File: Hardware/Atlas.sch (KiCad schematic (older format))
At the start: 47 parts, among them J1 DC, U1 MS5611, U2 HTU21D, U3 uSD Card, U4 RFD900, U5 MPU9150, U6 XBEE, U7 VENUS838FLPX-L, U8 AOZ1031

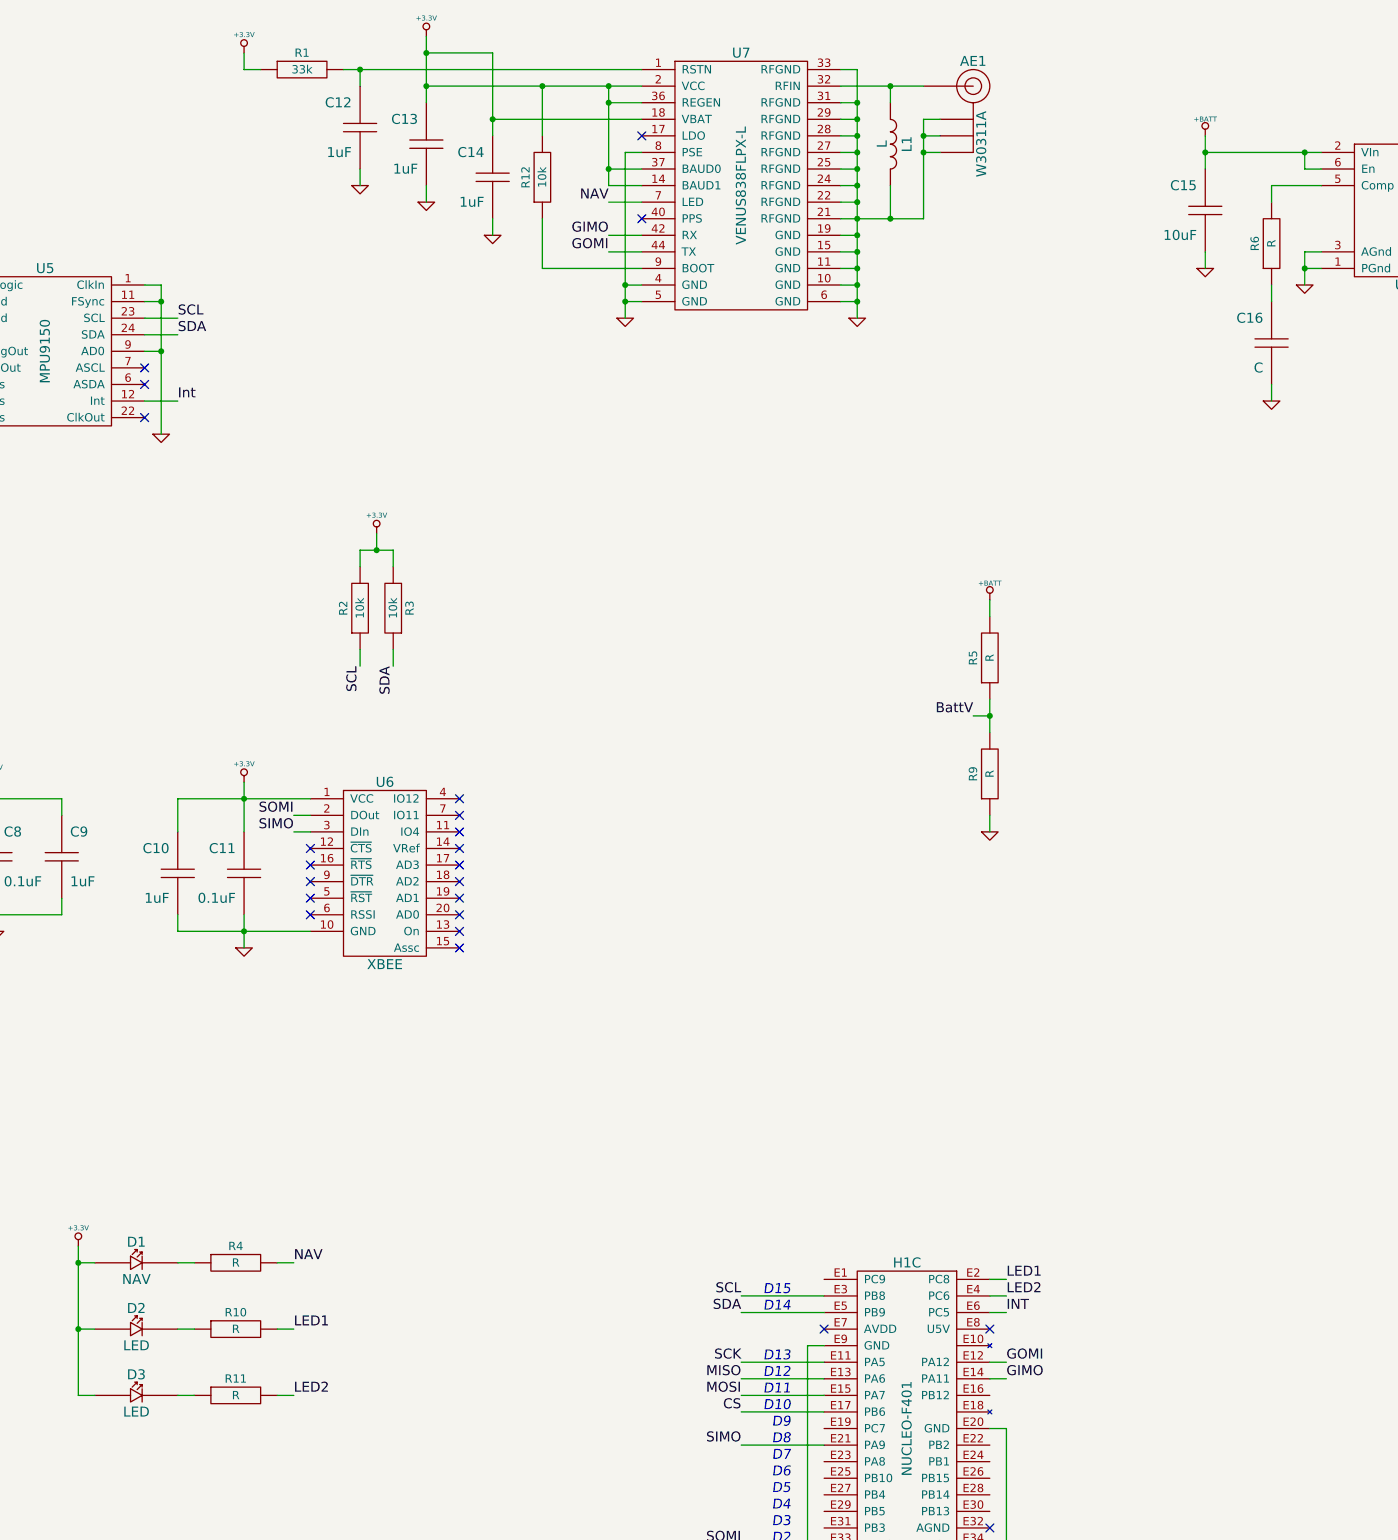
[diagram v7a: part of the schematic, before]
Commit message: Finish component values and BOM fields
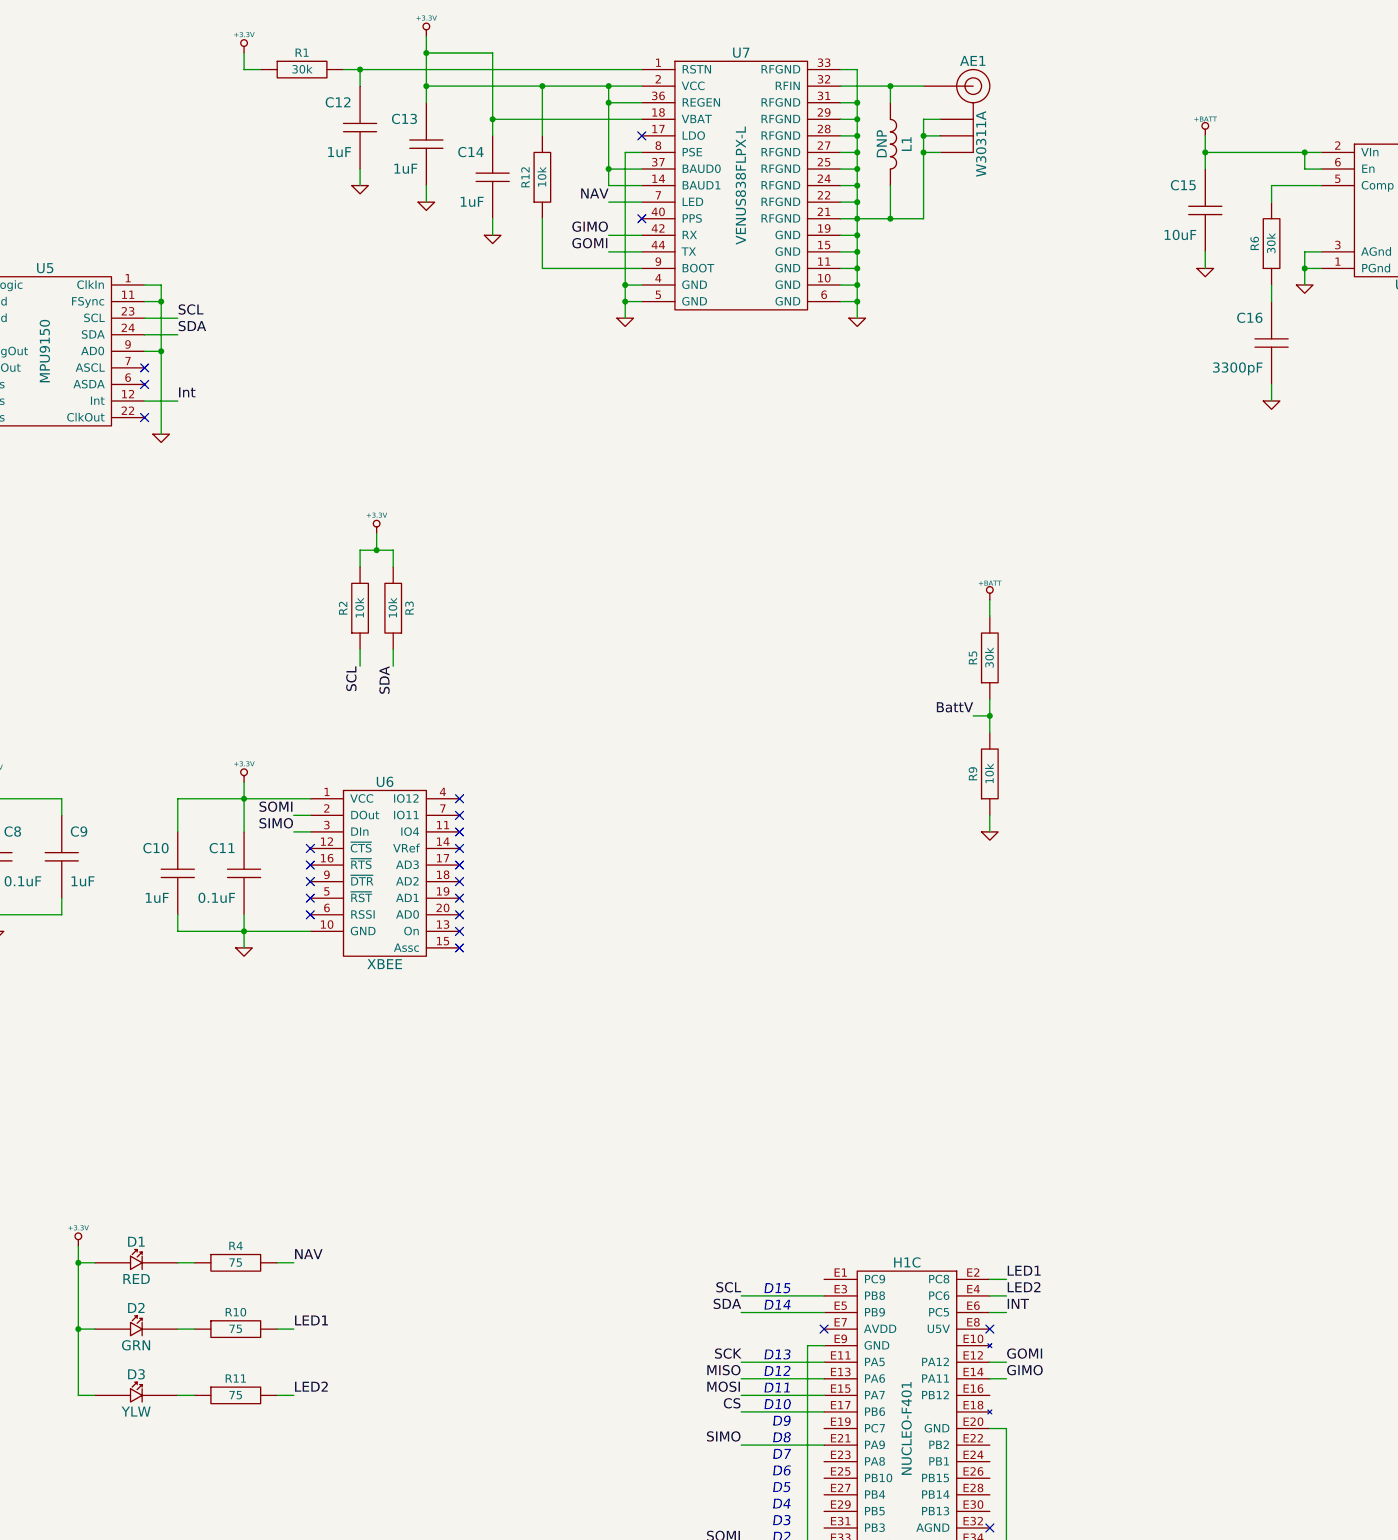
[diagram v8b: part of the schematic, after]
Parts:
- B1: Distributor Part No (none) -> 2477K-ND; MFR Name (none) -> Keystone; MFR Part No (none) -> 2477
- C16: value C -> 3300pF; footprint ~ -> CAPC1608-N; Dielectric D -> X7R; Distributor Part No (none) -> 1276-2034-1-ND; MFR Name (none) -> Samsung; MFR Part No (none) -> CL10B332KB8SFNC; Voltage V -> 50V
- D1: value NAV -> RED; footprint ~ -> LEDC1608-N; Current I -> 20mA; Distributor Part No (none) -> 475-3016-1-ND; MFR Name (none) -> Osram; MFR Part No (none) -> LS Q971-KN-1; Voltage V -> 1.9V
- D2: value LED -> GRN; footprint ~ -> LEDC1608-N; Current I -> 20mA; Distributor Part No (none) -> 475-1409-1-ND; MFR Name (none) -> Osram; MFR Part No (none) -> LG Q971-KN-1; Voltage V -> 2.2V
- D3: value LED -> YLW; footprint ~ -> LEDC1608-N; Current I -> 20mA; Distributor Part No (none) -> 475-2558-1-ND; MFR Name (none) -> Osram; MFR Part No (none) -> LY Q976-P1S2-36; Voltage V -> 2.0V
- J1: Distributor Part No (none) -> CP-202A-ND; MFR Name (none) -> CUI; MFR Part No (none) -> PJ-202A
- L1: value L -> DNP
- R1: value 33k -> 30k; footprint ~ -> RESC1608-N; Distributor Part No (none) -> RHM30KCGCT-ND; MFR Name (none) -> Rohm; MFR Part No (none) -> MCR03ERTJ303; Power W -> 1/10W; Tolerance % -> 5%
- R10, R11, R4: value R -> 75; footprint ~ -> RESC1608-N; Distributor Part No (none) -> RHM75CGCT-ND; MFR Name (none) -> Rohm; MFR Part No (none) -> MCR03ERTJ750; Power W -> 1/10W; Tolerance % -> 5%
- R5, R6: value R -> 30k; footprint ~ -> RESC1608-N; Distributor Part No (none) -> RHM30KCGCT-ND; MFR Name (none) -> Rohm; MFR Part No (none) -> MCR03ERTJ303; Power W -> 1/10W; Tolerance % -> 5%
- R9: value R -> 10k; footprint ~ -> RESC1608-N; Distributor Part No (none) -> RHM10KCGCT-ND; MFR Name (none) -> Rohm; MFR Part No (none) -> MCR03ERTJ103; Power W -> 1/10W; Tolerance % -> 5%
- U3: Distributor Part No (none) -> 101-00303-68-1-ND; MFR Name (none) -> Amphenol; MFR Part No (none) -> 101-00303-68
- U6: Distributor Part No (none) -> S5751-10-ND; MFR Name (none) -> Sullins; MFR Part No (none) -> NPPN101BFCN-RC
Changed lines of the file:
@@
 Sheet 1 1
 Title "Atlas (Nucleo Shield)"
-Date "1 jun 2014"
+Date "3 jun 2014"
 Rev "1"
 Comp "Aerodyne Labs"
@@
 F 2 "~" H 4000 1350 60  0000 C CNN
 F 3 "~" H 4000 1350 60  0000 C CNN
+F 4 "Amphenol" H 4000 1350 60  0001 C CNN "MFR Name"
+F 5 "101-00303-68" H 4000 1350 60  0001 C CNN "MFR Part No"
+F 6 "101-00303-68-1-ND" H 4000 1350 60  0001 C CNN "Distributor Part No"
 	1    4000 1350
 	-1   0    0    -1
@@
 F 2 "~" H 7800 5000 60  0000 C CNN
 F 3 "~" H 7800 5000 60  0000 C CNN
+F 4 "Sullins" H 7250 5950 60  0001 C CNN "MFR Name"
+F 5 "NPPN101BFCN-RC" H 7250 5950 60  0001 C CNN "MFR Part No"
+F 6 "S5751-10-ND" H 7250 5950 60  0001 C CNN "Distributor Part No"
 	1    7250 5950
 	1    0    0    -1
@@
 F 2 "~" H 14400 5850 60  0000 C CNN
 F 3 "~" H 14400 5850 60  0000 C CNN
+F 4 "Keystone" H 14400 5850 60  0001 C CNN "MFR Name"
+F 5 "2477" H 14400 5850 60  0001 C CNN "MFR Part No"
+F 6 "2477K-ND" H 14400 5850 60  0001 C CNN "Distributor Part No"
 	1    14400 5850
 	1    0    0    -1
@@
 F 3 "" H 14400 5400 60  0000 C CNN
 	1    14400 5400
-	1    0    0    -1
-$EndComp
-$Comp
-L R R1
-U 1 1 537F99E2
-P 6750 1100
-F 0 "R1" H 6750 1200 50  0000 C CNN
-F 1 "33k" H 6750 1100 50  0000 C CNN
-F 2 "~" H 6750 1100 60  0000 C CNN
-F 3 "~" H 6750 1100 60  0000 C CNN
-F 4 "W" H 6750 1000 50  0001 C CNN "Power"
-F 5 "%" H 6750 900 50  0001 C CNN "Tolerance"
-	1    6750 1100
 	1    0    0    -1
 $EndComp
@@
 P 5750 8300
 F 0 "D1" H 5750 8425 60  0000 C CNN
-F 1 "NAV" H 5750 8200 60  0000 C CNN
-F 2 "~" H 5750 8300 60  0000 C CNN
+F 1 "RED" H 5750 8200 60  0000 C CNN
+F 2 "LEDC1608-N" H 5750 8300 60  0001 C CNN
 F 3 "~" H 5750 8300 60  0000 C CNN
-F 4 "V" H 6150 8825 60  0001 C CNN "Voltage"
-F 5 "I" H 6250 8925 60  0001 C CNN "Current"
+F 4 "Osram" H 5750 8300 60  0001 C CNN "MFR Name"
+F 5 "LS Q971-KN-1" H 5750 8300 60  0001 C CNN "MFR Part No"
+F 6 "475-3016-1-ND" H 5750 8300 60  0001 C CNN "Distributor Part No"
+F 7 "1.9V" H 6150 8825 60  0001 C CNN "Voltage"
+F 8 "20mA" H 6250 8925 60  0001 C CNN "Current"
 	1    5750 8300
 	1    0    0    -1
@@
 P 6350 8300
 F 0 "R4" H 6350 8400 50  0000 C CNN
-F 1 "R" H 6350 8300 50  0000 C CNN
-F 2 "~" H 6350 8300 60  0000 C CNN
+F 1 "75" H 6350 8300 50  0000 C CNN
+F 2 "RESC1608-N" H 6350 8300 60  0001 C CNN
 F 3 "~" H 6350 8300 60  0000 C CNN
-F 4 "W" H 6350 8200 50  0001 C CNN "Power"
-F 5 "%" H 6350 8100 50  0001 C CNN "Tolerance"
+F 4 "Rohm" H 6350 8300 60  0001 C CNN "MFR Name"
+F 5 "MCR03ERTJ750" H 6350 8300 60  0001 C CNN "MFR Part No"
+F 6 "RHM75CGCT-ND" H 6350 8300 60  0001 C CNN "Distributor Part No"
+F 7 "1/10W" H 6350 8200 50  0001 C CNN "Power"
+F 8 "5%" H 6350 8100 50  0001 C CNN "Tolerance"
 	1    6350 8300
 	1    0    0    -1
@@
 P 10300 1550
 F 0 "L1" H 10300 1450 60  0000 C CNN
-F 1 "L" H 10300 1600 60  0000 C CNN
+F 1 "DNP" H 10300 1600 60  0000 C CNN
 F 2 "INDC1005-N" H 10300 1550 60  0001 C CNN
 F 3 "~" H 10300 1550 60  0000 C CNN
@@
 $EndComp
 $Comp
-L R R6
-U 1 1 53810165
-P 12600 2150
-F 0 "R6" H 12600 2250 50  0000 C CNN
-F 1 "R" H 12600 2150 50  0000 C CNN
-F 2 "~" H 12600 2150 60  0000 C CNN
-F 3 "~" H 12600 2150 60  0000 C CNN
-F 4 "W" H 12600 2050 50  0001 C CNN "Power"
-F 5 "%" H 12600 1950 50  0001 C CNN "Tolerance"
-	1    12600 2150
-	0    -1   -1   0
-$EndComp
-$Comp
 L C C16
 U 1 1 53810180
 P 12600 2750
 F 0 "C16" H 12650 2900 60  0000 L CNN
-F 1 "C" H 12650 2600 60  0000 L CNN
-F 2 "~" H 12600 2750 60  0000 C CNN
+F 1 "3300pF" H 12650 2600 60  0000 L CNN
+F 2 "CAPC1608-N" H 12600 2750 60  0001 C CNN
 F 3 "~" H 12600 2750 60  0000 C CNN
-F 4 "V" H 12550 2600 60  0001 R CNN "Voltage"
-F 5 "D" H 12550 2900 60  0001 R CNN "Dielectric"
+F 4 "Samsung" H 12600 2750 60  0001 C CNN "MFR Name"
+F 5 "CL10B332KB8SFNC" H 12600 2750 60  0001 C CNN "MFR Part No"
+F 6 "1276-2034-1-ND" H 12600 2750 60  0001 C CNN "Distributor Part No"
+F 7 "50V" H 12550 2600 60  0001 R CNN "Voltage"
+F 8 "X7R" H 12550 2900 60  0001 R CNN "Dielectric"
 	1    12600 2750
 	-1   0    0    -1
@@
 F 2 "~" H 13800 6200 60  0000 C CNN
 F 3 "~" H 13800 6200 60  0000 C CNN
+F 4 "CUI" H 13800 6200 60  0001 C CNN "MFR Name"
+F 5 "PJ-202A" H 13800 6200 60  0001 C CNN "MFR Part No"
+F 6 "CP-202A-ND" H 13800 6200 60  0001 C CNN "Distributor Part No"
 	1    13800 6200
 	1    0    0    -1
@@
 P 10900 4650
 F 0 "R5" H 10900 4750 50  0000 C CNN
-F 1 "R" H 10900 4650 50  0000 C CNN
-F 2 "~" H 10900 4650 60  0000 C CNN
+F 1 "30k" H 10900 4650 50  0000 C CNN
+F 2 "RESC1608-N" H 10900 4650 60  0001 C CNN
 F 3 "~" H 10900 4650 60  0000 C CNN
-F 4 "W" H 10900 4550 50  0001 C CNN "Power"
-F 5 "%" H 10900 4450 50  0001 C CNN "Tolerance"
+F 4 "Rohm" H 10900 4650 60  0001 C CNN "MFR Name"
+F 5 "MCR03ERTJ303" H 10900 4650 60  0001 C CNN "MFR Part No"
+F 6 "RHM30KCGCT-ND" H 10900 4650 60  0001 C CNN "Distributor Part No"
+F 7 "1/10W" H 10900 4550 50  0001 C CNN "Power"
+F 8 "5%" H 10900 4450 50  0001 C CNN "Tolerance"
 	1    10900 4650
-	0    -1   -1   0
-$EndComp
-$Comp
-L R R9
-U 1 1 53829234
-P 10900 5350
-F 0 "R9" H 10900 5450 50  0000 C CNN
-F 1 "R" H 10900 5350 50  0000 C CNN
-F 2 "~" H 10900 5350 60  0000 C CNN
-F 3 "~" H 10900 5350 60  0000 C CNN
-F 4 "W" H 10900 5250 50  0001 C CNN "Power"
-F 5 "%" H 10900 5150 50  0001 C CNN "Tolerance"
-	1    10900 5350
 	0    -1   -1   0
 $EndComp
@@
 P 5750 8700
 F 0 "D2" H 5750 8825 60  0000 C CNN
-F 1 "LED" H 5750 8600 60  0000 C CNN
-F 2 "~" H 5750 8700 60  0000 C CNN
+F 1 "GRN" H 5750 8600 60  0000 C CNN
+F 2 "LEDC1608-N" H 5750 8700 60  0001 C CNN
 F 3 "~" H 5750 8700 60  0000 C CNN
-F 4 "V" H 6150 9225 60  0001 C CNN "Voltage"
-F 5 "I" H 6250 9325 60  0001 C CNN "Current"
+F 4 "Osram" H 5750 8700 60  0001 C CNN "MFR Name"
+F 5 "LG Q971-KN-1" H 5750 8700 60  0001 C CNN "MFR Part No"
+F 6 "475-1409-1-ND" H 5750 8700 60  0001 C CNN "Distributor Part No"
+F 7 "2.2V" H 6150 9225 60  0001 C CNN "Voltage"
+F 8 "20mA" H 6250 9325 60  0001 C CNN "Current"
 	1    5750 8700
-	1    0    0    -1
-$EndComp
-$Comp
-L R R10
-U 1 1 5382B2F0
-P 6350 8700
-F 0 "R10" H 6350 8800 50  0000 C CNN
-F 1 "R" H 6350 8700 50  0000 C CNN
-F 2 "~" H 6350 8700 60  0000 C CNN
-F 3 "~" H 6350 8700 60  0000 C CNN
-F 4 "W" H 6350 8600 50  0001 C CNN "Power"
-F 5 "%" H 6350 8500 50  0001 C CNN "Tolerance"
-	1    6350 8700
-	1    0    0    -1
-$EndComp
-$Comp
-L R R11
-U 1 1 5382B30B
-P 6350 9100
-F 0 "R11" H 6350 9200 50  0000 C CNN
-F 1 "R" H 6350 9100 50  0000 C CNN
-F 2 "~" H 6350 9100 60  0000 C CNN
-F 3 "~" H 6350 9100 60  0000 C CNN
-F 4 "W" H 6350 9000 50  0001 C CNN "Power"
-F 5 "%" H 6350 8900 50  0001 C CNN "Tolerance"
-	1    6350 9100
 	1    0    0    -1
 $EndComp
@@
 P 5750 9100
 F 0 "D3" H 5750 9225 60  0000 C CNN
-F 1 "LED" H 5750 9000 60  0000 C CNN
-F 2 "~" H 5750 9100 60  0000 C CNN
+F 1 "YLW" H 5750 9000 60  0000 C CNN
+F 2 "LEDC1608-N" H 5750 9100 60  0001 C CNN
 F 3 "~" H 5750 9100 60  0000 C CNN
-F 4 "V" H 6150 9625 60  0001 C CNN "Voltage"
-F 5 "I" H 6250 9725 60  0001 C CNN "Current"
+F 4 "Osram" H 5750 9100 60  0001 C CNN "MFR Name"
+F 5 "LY Q976-P1S2-36" H 5750 9100 60  0001 C CNN "MFR Part No"
+F 6 "475-2558-1-ND" H 5750 9100 60  0001 C CNN "Distributor Part No"
+F 7 "2.0V" H 6150 9625 60  0001 C CNN "Voltage"
+F 8 "20mA" H 6250 9725 60  0001 C CNN "Current"
 	1    5750 9100
 	1    0    0    -1
@@
 	0    -1   -1   0
 $EndComp
+$Comp
+L R R9
+U 1 1 538DCD2E
+P 10900 5350
+F 0 "R9" H 10900 5450 50  0000 C CNN
+F 1 "10k" H 10900 5350 50  0000 C CNN
+F 2 "RESC1608-N" H 10900 5350 60  0001 C CNN
+F 3 "~" H 10900 5350 60  0000 C CNN
+F 4 "Rohm" H 10900 5350 60  0001 C CNN "MFR Name"
+F 5 "MCR03ERTJ103" H 10900 5350 60  0001 C CNN "MFR Part No"
+F 6 "RHM10KCGCT-ND" H 10900 5350 60  0001 C CNN "Distributor Part No"
+F 7 "1/10W" H 10900 5250 50  0001 C CNN "Power"
+F 8 "5%" H 10900 5150 50  0001 C CNN "Tolerance"
+	1    10900 5350
+	0    -1   -1   0
+$EndComp
+$Comp
+L R R6
+U 1 1 538DD812
+P 12600 2150
+F 0 "R6" H 12600 2250 50  0000 C CNN
+F 1 "30k" H 12600 2150 50  0000 C CNN
+F 2 "RESC1608-N" H 12600 2150 60  0001 C CNN
+F 3 "~" H 12600 2150 60  0000 C CNN
+F 4 "Rohm" H 12600 2150 60  0001 C CNN "MFR Name"
+F 5 "MCR03ERTJ303" H 12600 2150 60  0001 C CNN "MFR Part No"
+F 6 "RHM30KCGCT-ND" H 12600 2150 60  0001 C CNN "Distributor Part No"
+F 7 "1/10W" H 12600 2050 50  0001 C CNN "Power"
+F 8 "5%" H 12600 1950 50  0001 C CNN "Tolerance"
+	1    12600 2150
+	0    -1   -1   0
+$EndComp
+$Comp
+L R R10
+U 1 1 538DE219
+P 6350 8700
+F 0 "R10" H 6350 8800 50  0000 C CNN
+F 1 "75" H 6350 8700 50  0000 C CNN
+F 2 "RESC1608-N" H 6350 8700 60  0001 C CNN
+F 3 "~" H 6350 8700 60  0000 C CNN
+F 4 "Rohm" H 6350 8700 60  0001 C CNN "MFR Name"
+F 5 "MCR03ERTJ750" H 6350 8700 60  0001 C CNN "MFR Part No"
+F 6 "RHM75CGCT-ND" H 6350 8700 60  0001 C CNN "Distributor Part No"
+F 7 "1/10W" H 6350 8600 50  0001 C CNN "Power"
+F 8 "5%" H 6350 8500 50  0001 C CNN "Tolerance"
+	1    6350 8700
+	1    0    0    -1
+$EndComp
+$Comp
+L R R11
+U 1 1 538DE224
+P 6350 9100
+F 0 "R11" H 6350 9200 50  0000 C CNN
+F 1 "75" H 6350 9100 50  0000 C CNN
+F 2 "RESC1608-N" H 6350 9100 60  0001 C CNN
+F 3 "~" H 6350 9100 60  0000 C CNN
+F 4 "Rohm" H 6350 9100 60  0001 C CNN "MFR Name"
+F 5 "MCR03ERTJ750" H 6350 9100 60  0001 C CNN "MFR Part No"
+F 6 "RHM75CGCT-ND" H 6350 9100 60  0001 C CNN "Distributor Part No"
+F 7 "1/10W" H 6350 9000 50  0001 C CNN "Power"
+F 8 "5%" H 6350 8900 50  0001 C CNN "Tolerance"
+	1    6350 9100
+	1    0    0    -1
+$EndComp
+$Comp
+L R R1
+U 1 1 538DEB3D
+P 6750 1100
+F 0 "R1" H 6750 1200 50  0000 C CNN
+F 1 "30k" H 6750 1100 50  0000 C CNN
+F 2 "RESC1608-N" H 6750 1100 60  0001 C CNN
+F 3 "~" H 6750 1100 60  0000 C CNN
+F 4 "Rohm" H 6750 1100 60  0001 C CNN "MFR Name"
+F 5 "MCR03ERTJ303" H 6750 1100 60  0001 C CNN "MFR Part No"
+F 6 "RHM30KCGCT-ND" H 6750 1100 60  0001 C CNN "Distributor Part No"
+F 7 "1/10W" H 6750 1000 50  0001 C CNN "Power"
+F 8 "5%" H 6750 900 50  0001 C CNN "Tolerance"
+	1    6750 1100
+	1    0    0    -1
+$EndComp
 $EndSCHEMATC
